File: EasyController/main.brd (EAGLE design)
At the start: 90 x 76 mm, 50 parts, among them IC2 L6387EDIP8, IC3 L6387EDIP8, IC4 L6387EDIP8, J3 FUSE

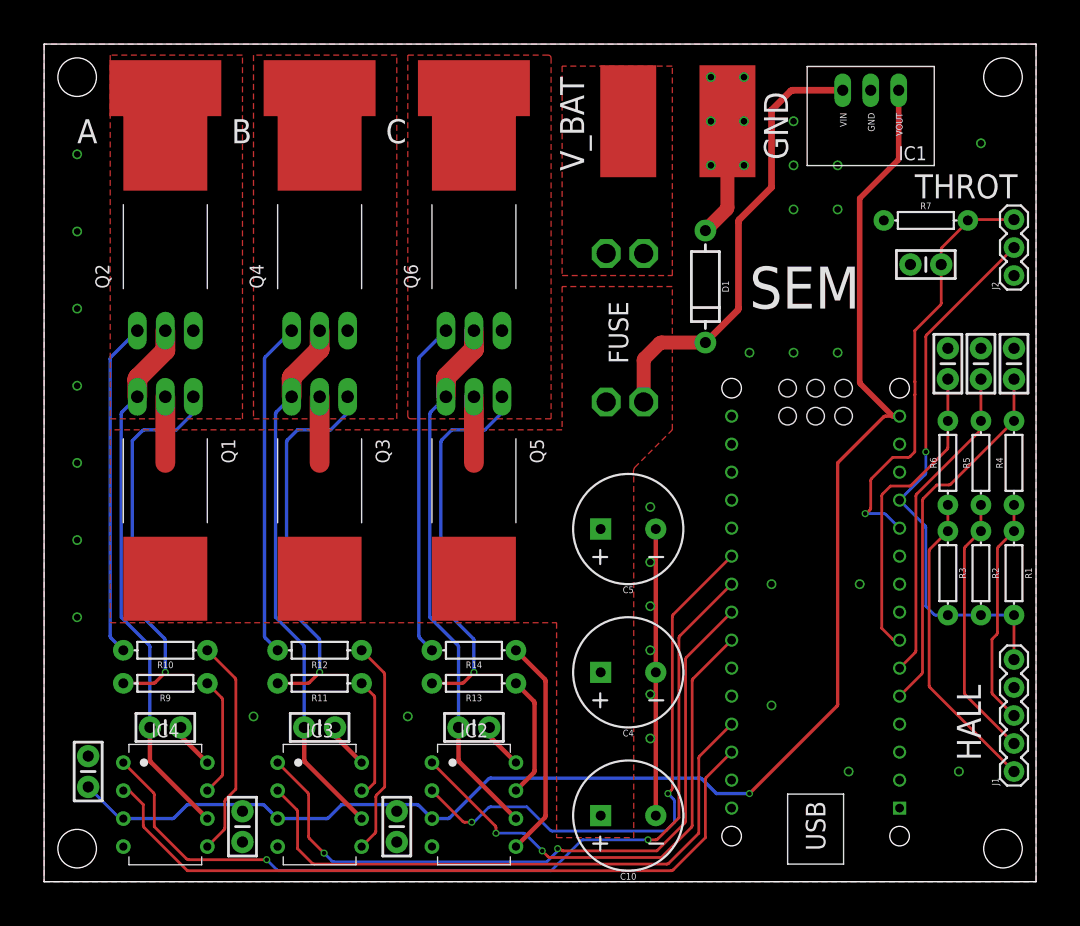
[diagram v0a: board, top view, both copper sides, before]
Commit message: EasyController and EasyTelemetry almost ready to submit
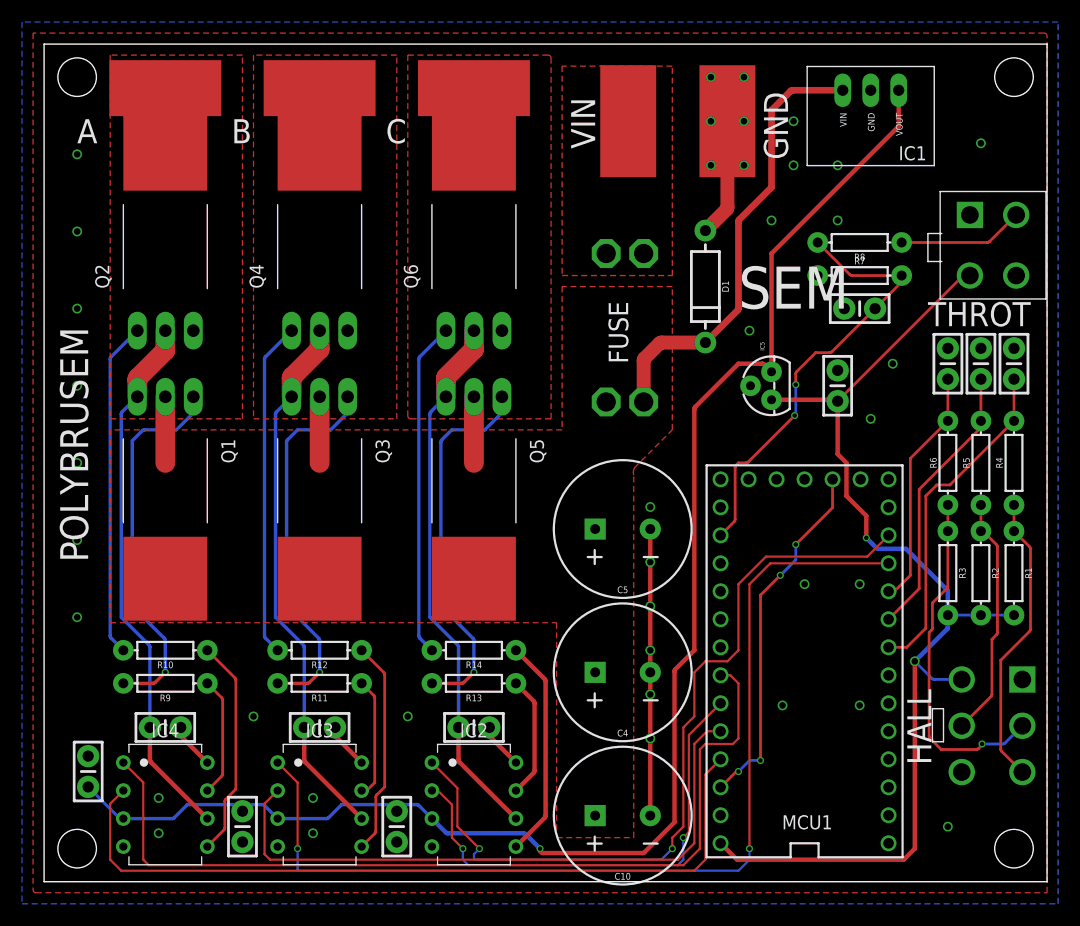
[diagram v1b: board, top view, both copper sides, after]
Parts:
- removed J1: (no value), SparkFun-Connectors:1X05
- removed J2: (no value), SparkFun-Connectors:1X03
- added C14: 1uF, SparkFun-Capacitors:CAP-PTH-SMALL-KIT
- added IC5: (no value), SparkFun-IC-Power:TO-92
- added R8: 47k, SparkFun-Resistors:AXIAL-0.3
- added U$1: HEADER4VALULOK, Custom_old:4PINVALULOK
- added U$2: HEADER6, Custom_old:6PINVALULOK
- C10, C4, C5: value 680uF -> 470uF
- C9: value 1uF -> 47nF
- MCU1: device ArduinoNanoV30:ARDUINO_NANO -> Teensy3.0:TEENSY_3.0_BASIC
- moved R7 7.81 mm to (74.0, 55.0)
- moved C9 7.21 mm to (74.0, 52.0)
- moved MCU1 7.07 mm to (69.0, 20.0), turned to 180 degrees
- moved U$10 1.00 mm to (88.0, 73.0)
- moved U$11 1.00 mm to (88.0, 3.00)
- moved C10 0.50 mm to (52.5, 6.00)
- moved C4 0.50 mm to (52.5, 19.0)
- moved C5 0.50 mm to (52.5, 32.0)
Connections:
- new net 3.3V: MCU1.3.3V, MCU1.3.3V1
- new net N$7: R8.P$1, U$1.3
- new net VBAT: MCU1.VBAT
- net 5V: now also C14.1, IC5.1, MCU1.VIN, U$1.2, U$2.2; no longer J1.5, J2.2, MCU1.12
- net CTRL_AH: now also MCU1.23/A9; no longer MCU1.28
- net CTRL_AL: now also MCU1.20/A6; no longer MCU1.22
- net CTRL_BH: now also MCU1.22/A8; no longer MCU1.27
- net CTRL_BL: now also MCU1.9; no longer MCU1.23
- net CTRL_CH: now also MCU1.21/A7; no longer MCU1.21
- net CTRL_CL: now also MCU1.10; no longer MCU1.24
- net GND: now also C14.2, IC5.2, MCU1.AGND, MCU1.GND, MCU1.GND1, U$1.4, U$2.1; no longer J1.4, J2.1, MCU1.14, MCU1.19
- net HALL_A: now also MCU1.6; no longer MCU1.5
- net HALL_B: now also MCU1.7; no longer MCU1.6
- net HALL_C: now also MCU1.8; no longer MCU1.7
- net N$2: now also U$2.3; no longer J1.1
- net N$4: now also U$2.4; no longer J1.2
- net N$6: now also U$2.5; no longer J1.3
- net THROTTLE: now also MCU1.15/A1, R8.P$2; no longer J2.3, MCU1.11
- net VDD: now also IC5.3; no longer MCU1.15
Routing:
- net 5V: track 50.1 -> 99.8 mm, vias 1 -> 2
- net 3.3V: track 0.00 -> 33.0 mm, vias 0 -> 4
- net CTRL_CL: track 47.0 -> 72.3 mm
- net CTRL_BL: track 65.8 -> 90.4 mm
- net N$7: track 0.00 -> 11.4 mm
- net CTRL_CH: track 51.7 -> 43.8 mm
- net HALL_C: track 28.1 -> 21.8 mm
- net N$6: track 20.7 -> 26.7 mm
- net CTRL_AH: track 66.9 -> 71.3 mm
- net HALL_B: track 29.2 -> 25.3 mm
- net N$2: track 28.1 -> 31.6 mm, vias 0 -> 1
- net HALL_A: track 33.7 -> 30.7 mm
- net CTRL_BH: track 55.2 -> 57.9 mm
- net N$4: track 24.1 -> 22.1 mm
- net VDD: track 139.4 -> 137.7 mm
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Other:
- board size 90 x 76 mm -> 91 x 76 mm
- board text added: "BLDC Controller 1.1 Designed by PLG, Feb 2019 POLYBRUSEM, Shell Eco-Marathon"
- board text added: "POLYBRUSEM"
- board text added: "VIN"
- board text removed: "EasyController 1.0 Designed by Patrick Grady Jan 2019"
- board text removed: "V_BAT"

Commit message: Allpcb submit
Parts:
- moved U$1 4.85 mm to (83.3, 59.8), turned to 270 degrees
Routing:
- net 5V: track 99.8 -> 104.0 mm
- net N$7: track 11.4 -> 12.0 mm
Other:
- board text added: "+5V"
- board text added: "HALL A"
- board text added: "HALL B"
- board text added: "HALL C"
- board text removed: "5v GND HALL A HALL B HALL C"
- board text removed: "THROTTLE 5v GND"
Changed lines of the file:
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@@
 <wire x1="91" y1="76" x2="0" y2="76" width="0" layer="20"/>
 <wire x1="0" y1="76" x2="0" y2="0" width="0" layer="20"/>
-<text x="63" y="52" size="3.81" layer="21">SEM</text>
+<text x="67" y="50" size="3.81" layer="21" rot="R90">SEM</text>
 <text x="45" y="64" size="3.81" layer="22" rot="MR0">SEM</text>
 <text x="45" y="55" size="1.778" layer="22" rot="MR0">BLDC Controller 1.1
 Designed by PLG, Feb 2019
 POLYBRUSEM, Shell Eco-Marathon</text>
-<text x="86.5" y="9" size="1.778" layer="22" rot="MR0">5v
-GND
-HALL A
-HALL B
-HALL C</text>
-<text x="86" y="54" size="1.778" layer="22" rot="MR0">THROTTLE
-5v
-GND</text>
 <text x="53" y="47" size="1.778" layer="21" rot="R90">FUSE</text>
 <text x="3" y="67" size="2.1844" layer="21">A</text>
@@
 <text x="80.2" y="50.4" size="2.1844" layer="21">THROT</text>
 <text x="4" y="29" size="2.54" layer="21" rot="R90">POLYBRUSEM</text>
+<text x="87" y="20" size="1.016" layer="22" rot="MR270">GND</text>
+<text x="81" y="20" size="1.016" layer="22" rot="MR270">+5V</text>
+<text x="87" y="11" size="0.8128" layer="22" rot="MR270">HALL A</text>
+<text x="81" y="16" size="1.016" layer="22" rot="MR270">HALL B</text>
+<text x="87" y="16" size="0.8128" layer="22" rot="MR270">HALL C</text>
+<text x="81.2" y="60.6" size="0.8128" layer="22" rot="MR270">+5V</text>
+<text x="81.2" y="56.5" size="0.8128" layer="22" rot="MR270">GND</text>
+<text x="87" y="57" size="0.8128" layer="22" rot="MR270">THROT</text>
 </plain>
 <attributes>
@@
 <attribute name="PROD_ID" value=" " x="74" y="58" size="1.778" layer="27" rot="R180" display="off"/>
 </element>
-<element name="U$1" library="Custom_old" package="4PINVALULOK" value="HEADER4VALULOK" x="84" y="55"/>
+<element name="U$1" library="Custom_old" package="4PINVALULOK" value="HEADER4VALULOK" x="83.3" y="59.8" rot="R270"/>
 <element name="U$2" library="Custom_old" package="6PINVALULOK" value="HEADER6" x="85.8" y="12" rot="R270"/>
 </elements>
@@
 <wire x1="80.57560625" y1="18.42439375" x2="80.755209375" y2="18.35" width="0.254" layer="16" curve="44.999295"/>
 <wire x1="80.755209375" y1="18.35" x2="83.26" y2="18.35" width="0.254" layer="16"/>
-<wire x1="72" y1="43.603" x2="83.32260625" y2="54.92560625" width="0.254" layer="1"/>
-<wire x1="83.32260625" y1="54.92560625" x2="83.502209375" y2="55" width="0.254" layer="1" curve="-44.999295"/>
-<wire x1="83.502209375" y1="55" x2="84" y2="55" width="0.254" layer="1"/>
+<wire x1="72" y1="43.603" x2="75" y2="46.603" width="0.4064" layer="1"/>
+<wire x1="75" y1="46.603" x2="75" y2="48" width="0.4064" layer="1"/>
+<wire x1="75" y1="48" x2="80" y2="53" width="0.4064" layer="1"/>
+<wire x1="80" y1="56.5" x2="83.3" y2="59.8" width="0.4064" layer="1"/>
+<wire x1="80" y1="53" x2="80" y2="56.5" width="0.4064" layer="1"/>
 </signal>
 <signal name="HALL_A">
@@
 <contactref element="R8" pad="P$1"/>
 <contactref element="U$1" pad="3"/>
-<wire x1="77.81" y1="58" x2="85.594790625" y2="58" width="0.254" layer="1"/>
-<wire x1="88.2" y1="60.5" x2="85.77439375" y2="58.07439375" width="0.254" layer="1"/>
-<wire x1="85.77439375" y1="58.07439375" x2="85.594790625" y2="58" width="0.254" layer="1" curve="-44.999295"/>
+<wire x1="77.81" y1="58" x2="80.9" y2="58" width="0.4064" layer="16"/>
+<wire x1="80.9" y1="58" x2="81.5" y2="57.4" width="0.4064" layer="16"/>
+<wire x1="81.5" y1="57.4" x2="87" y2="57.4" width="0.4064" layer="16"/>
+<wire x1="87" y1="57.4" x2="88.8" y2="55.6" width="0.4064" layer="16"/>
 </signal>
 </signals>
